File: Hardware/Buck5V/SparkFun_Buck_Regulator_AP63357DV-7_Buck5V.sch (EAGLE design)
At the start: 29 parts, among them J3 POWER_JACK, U1 AP63357

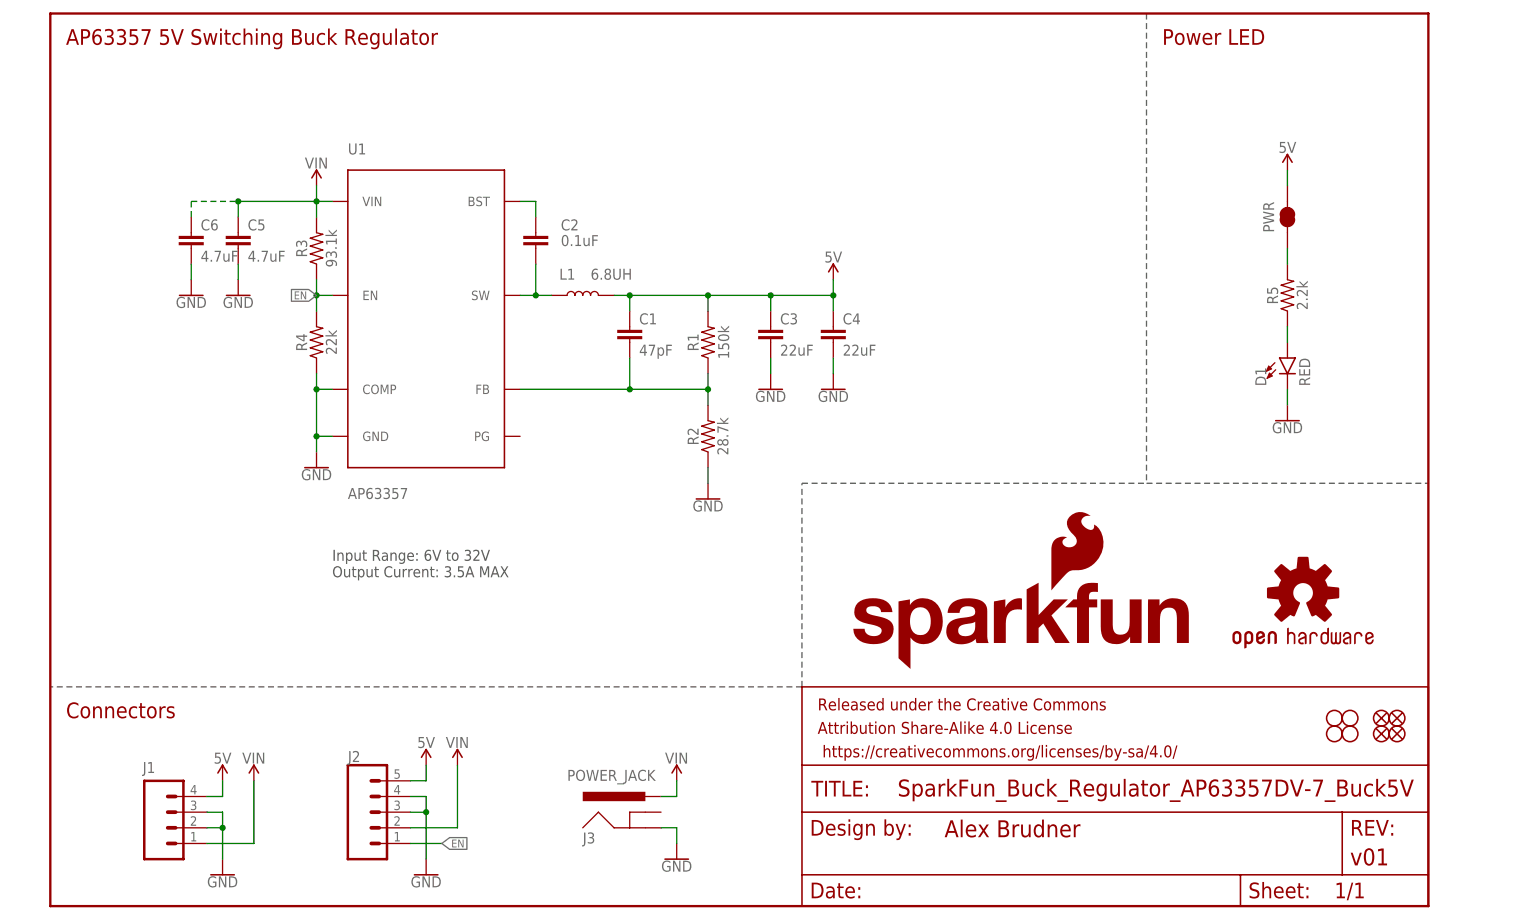
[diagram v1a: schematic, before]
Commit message: v01 changes implemented.
Schematic:
Add note for LED jumper
Add green wire for EN
Section titles center anchor
Rename Regulator section
Layout:
Increase selective solder width
Move 1x1 thermal pad
Make silk labels more explicit
Add "CAUTION: HOT" or just "HOT" silk
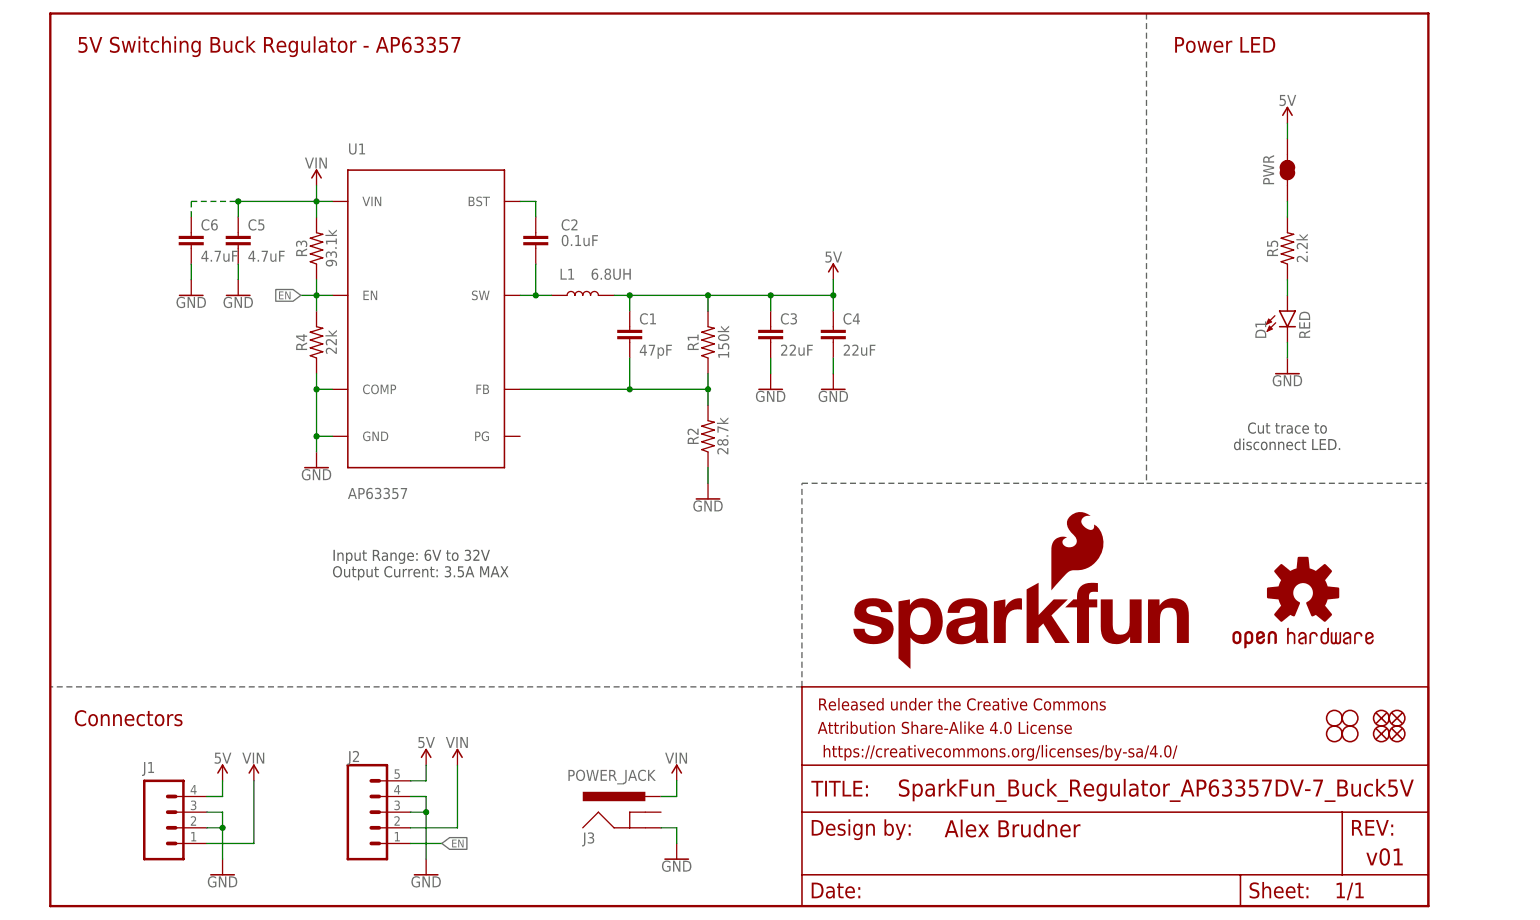
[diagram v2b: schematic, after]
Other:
- note added: "5V Switching Buck Regulator - AP63357"
- note added: "Cut trace to disconnect LED."
- note removed: "AP63357 5V Switching Buck Regulator"
- moved on the sheet: D1, PWR, R5
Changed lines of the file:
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@@
 <setting verticaltext="up"/>
 </settings>
-<grid distance="0.1" unitdist="inch" unit="inch" style="lines" multiple="1" display="no" altdistance="0.01" altunitdist="inch" altunit="inch"/>
+<grid distance="0.1" unitdist="inch" unit="inch" style="lines" multiple="1" display="yes" altdistance="0.01" altunitdist="inch" altunit="inch"/>
 <layers>
 <layer number="1" name="Top" color="4" fill="1" visible="no" active="no"/>
@@
 <wire x1="177.8" y1="68.58" x2="223.52" y2="68.58" width="0.2032" layer="97" style="longdash"/>
 <wire x1="121.92" y1="35.56" x2="0" y2="35.56" width="0.2032" layer="97" style="longdash"/>
-<text x="180.34" y="139.7" size="2.54" layer="94" font="vector">Power LED</text>
+<text x="190.5" y="139.7" size="2.54" layer="94" font="vector" align="center">Power LED</text>
 <wire x1="177.8" y1="144.78" x2="177.8" y2="68.58" width="0.2032" layer="97" style="longdash"/>
-<text x="2.54" y="30.48" size="2.54" layer="94" font="vector">Connectors</text>
-<text x="2.54" y="139.7" size="2.54" layer="94" font="vector">AP63357 5V Switching Buck Regulator</text>
+<text x="12.7" y="30.48" size="2.54" layer="94" font="vector" align="center">Connectors</text>
+<text x="35.56" y="139.7" size="2.54" layer="94" font="vector" align="center">5V Switching Buck Regulator - AP63357</text>
 <text x="45.72" y="53.34" size="1.778" layer="97" font="vector">Input Range: 6V to 32V
 Output Current: 3.5A MAX</text>
+<text x="200.66" y="76.2" size="1.778" layer="97" font="vector" align="center">Cut trace to
+disconnect LED.</text>
 </plain>
 <instances>
@@
 <attribute name="DRAWING_NAME" x="137.414" y="17.78" size="2.7432" layer="94" font="vector"/>
 <attribute name="DESIGNER" x="145.034" y="11.176" size="2.7432" layer="94" font="vector"/>
-<attribute name="REV" x="210.82" y="6.604" size="2.7432" layer="94" font="vector"/>
+<attribute name="REV" x="213.36" y="6.604" size="2.7432" layer="94" font="vector"/>
 </instance>
 <instance part="FD1" gate="G$1" x="218.44" y="30.48" smashed="yes"/>
@@
 <attribute name="VALUE" x="101.6" y="7.366" size="1.778" layer="96" font="vector" align="top-center"/>
 </instance>
-<instance part="SUPPLY8" gate="G$1" x="200.66" y="119.38" smashed="yes">
-<attribute name="VALUE" x="200.66" y="122.174" size="1.778" layer="96" font="vector" align="bottom-center"/>
-</instance>
-<instance part="PWR" gate="G$1" x="200.66" y="111.76" smashed="yes" rot="R90">
-<attribute name="NAME" x="197.612" y="111.76" size="1.778" layer="95" font="vector" rot="R90" align="center"/>
-</instance>
-<instance part="D1" gate="G$1" x="200.66" y="88.9" smashed="yes">
-<attribute name="NAME" x="197.231" y="84.328" size="1.778" layer="95" font="vector" rot="R90"/>
-<attribute name="VALUE" x="202.565" y="84.328" size="1.778" layer="96" font="vector" rot="R90" align="top-left"/>
-</instance>
-<instance part="R5" gate="G$1" x="200.66" y="99.06" smashed="yes" rot="R90">
-<attribute name="NAME" x="199.136" y="99.06" size="1.778" layer="95" font="vector" rot="R90" align="bottom-center"/>
-<attribute name="VALUE" x="202.184" y="99.06" size="1.778" layer="96" font="vector" rot="R90" align="top-center"/>
-</instance>
-<instance part="GND9" gate="1" x="200.66" y="78.74" smashed="yes">
-<attribute name="VALUE" x="200.66" y="78.486" size="1.778" layer="96" font="vector" align="top-center"/>
+<instance part="SUPPLY8" gate="G$1" x="200.66" y="127" smashed="yes">
+<attribute name="VALUE" x="200.66" y="129.794" size="1.778" layer="96" font="vector" align="bottom-center"/>
+</instance>
+<instance part="PWR" gate="G$1" x="200.66" y="119.38" smashed="yes" rot="R90">
+<attribute name="NAME" x="197.612" y="119.38" size="1.778" layer="95" font="vector" rot="R90" align="center"/>
+</instance>
+<instance part="D1" gate="G$1" x="200.66" y="96.52" smashed="yes">
+<attribute name="NAME" x="197.231" y="91.948" size="1.778" layer="95" font="vector" rot="R90"/>
+<attribute name="VALUE" x="202.565" y="91.948" size="1.778" layer="96" font="vector" rot="R90" align="top-left"/>
+</instance>
+<instance part="R5" gate="G$1" x="200.66" y="106.68" smashed="yes" rot="R90">
+<attribute name="NAME" x="199.136" y="106.68" size="1.778" layer="95" font="vector" rot="R90" align="bottom-center"/>
+<attribute name="VALUE" x="202.184" y="106.68" size="1.778" layer="96" font="vector" rot="R90" align="top-center"/>
+</instance>
+<instance part="GND9" gate="1" x="200.66" y="86.36" smashed="yes">
+<attribute name="VALUE" x="200.66" y="86.106" size="1.778" layer="96" font="vector" align="top-center"/>
 </instance>
 <instance part="LOGO1" gate="G$1" x="203.2" y="50.8" smashed="yes"/>
@@
 <segment>
 <pinref part="GND9" gate="1" pin="GND"/>
-<wire x1="200.66" y1="83.82" x2="200.66" y2="81.28" width="0.1524" layer="91"/>
+<wire x1="200.66" y1="91.44" x2="200.66" y2="88.9" width="0.1524" layer="91"/>
 <pinref part="D1" gate="G$1" pin="C"/>
 </segment>
@@
 <wire x1="43.18" y1="96.52" x2="43.18" y2="99.06" width="0.1524" layer="91"/>
 <junction x="43.18" y="99.06"/>
-<label x="43.18" y="99.06" size="1.27" layer="95" rot="R180" xref="yes"/>
+<label x="40.64" y="99.06" size="1.27" layer="95" rot="R180" xref="yes"/>
+<wire x1="40.64" y1="99.06" x2="43.18" y2="99.06" width="0.1524" layer="91"/>
 </segment>
 <segment>
@@
 <segment>
 <pinref part="SUPPLY8" gate="G$1" pin="5V"/>
-<wire x1="200.66" y1="116.84" x2="200.66" y2="119.38" width="0.1524" layer="91"/>
+<wire x1="200.66" y1="124.46" x2="200.66" y2="127" width="0.1524" layer="91"/>
 <pinref part="PWR" gate="G$1" pin="2"/>
 </segment>
@@
 <pinref part="D1" gate="G$1" pin="A"/>
 <pinref part="R5" gate="G$1" pin="1"/>
-<wire x1="200.66" y1="91.44" x2="200.66" y2="93.98" width="0.1524" layer="91"/>
+<wire x1="200.66" y1="99.06" x2="200.66" y2="101.6" width="0.1524" layer="91"/>
 </segment>
 </net>
@@
 <pinref part="R5" gate="G$1" pin="2"/>
 <pinref part="PWR" gate="G$1" pin="1"/>
-<wire x1="200.66" y1="104.14" x2="200.66" y2="106.68" width="0.1524" layer="91"/>
-</segment>
-</net>
+<wire x1="200.66" y1="111.76" x2="200.66" y2="114.3" width="0.1524" layer="91"/>
+</segment>
+</net>

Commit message: Remove silk from Power Jack so no silk overhangs.
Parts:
- J3: device SparkFun-Connectors:POWER_JACKPOWER_JACK_SLOT -> SparkFun-Connectors:POWER_JACKPOWER_JACK_SLOT_NO_SILK_OVRHNG
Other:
- note added: "UVLO Hi: 5.6V UVLO Lo: 5.18V See Datasheet pg 15 Eq. 2+3 For calculating R3/R4"
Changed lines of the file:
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@@
 <part name="FD4" library="SparkFun-Aesthetics" deviceset="FIDUCIAL" device="UFIDUCIAL"/>
 <part name="J1" library="SparkFun-Connectors" deviceset="CONN_04" device="SCREW"/>
-<part name="J3" library="SparkFun-Connectors" deviceset="POWER_JACK" device="POWER_JACK_SLOT" value="POWER_JACK"/>
+<part name="J3" library="SparkFun-Connectors" deviceset="POWER_JACK" device="POWER_JACK_SLOT_NO_SILK_OVRHNG" value="POWER_JACK"/>
 <part name="J2" library="SparkFun-Connectors" deviceset="CONN_05" device="NO_SILK"/>
 <part name="R2" library="Buck5V" deviceset="28.7KOHM" device="-0402-1/16W-1%(28.7KOHM)" value="28.7k"/>
@@
 <text x="200.66" y="76.2" size="1.778" layer="97" font="vector" align="center">Cut trace to
 disconnect LED.</text>
+<text x="5.08" y="83.82" size="1.778" layer="97" font="vector" align="center-left">UVLO Hi: 5.6V
+UVLO Lo: 5.18V
+See Datasheet pg 15 Eq. 2+3
+For calculating R3/R4</text>
 </plain>
 <instances>
